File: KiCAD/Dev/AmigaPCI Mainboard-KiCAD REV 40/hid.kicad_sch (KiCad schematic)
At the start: 48 parts, among them CN201 USB_A_Stacked, CN202 DB9_Male_Stack, CN227 JTAG/SWD, U221 74HCT4066, U222 74HCT4066, U223 74HCT245, U224 74AHCT157, U225 USBLC6-2SC6, U226 USBLC6-2SC6, U227 STM32F205RET7, U228 AP2156SG-13, Y2 32.768KHz, Y3 25MHz

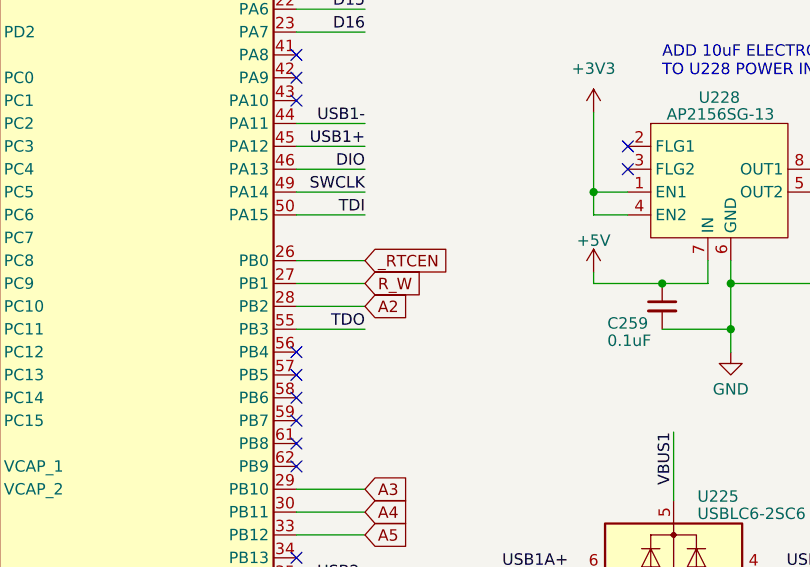
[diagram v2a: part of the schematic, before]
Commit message: AmigaPCI Rev 4.0 Routing
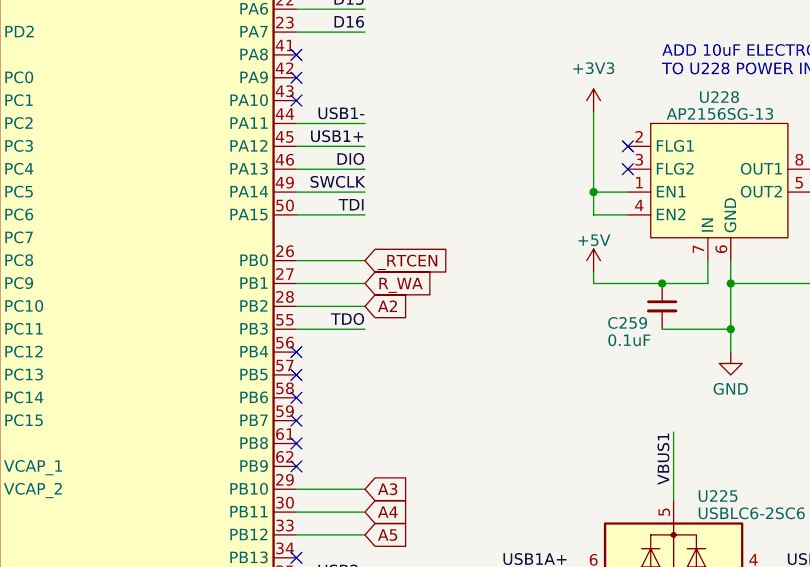
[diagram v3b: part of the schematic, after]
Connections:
- net R_W renamed R_WA
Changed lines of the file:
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@@
 		)
 	)
-	(global_label "R_W"
+	(global_label "R_WA"
 		(shape input)
 		(at 294.64 102.87 0)
@@
 		)
 		(property "Intersheetrefs" "${INTERSHEET_REFS}"
-			(at 301.3142 102.87 0)
+			(at 302.4028 102.87 0)
 			(effects
 				(font
